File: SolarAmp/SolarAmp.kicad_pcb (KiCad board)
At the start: 2 copper layers, 45.5 x 19 mm, 12 parts, among them J1 Sound Input, J2 Speaker Out, J3 Power Input, U1 TDA2822M

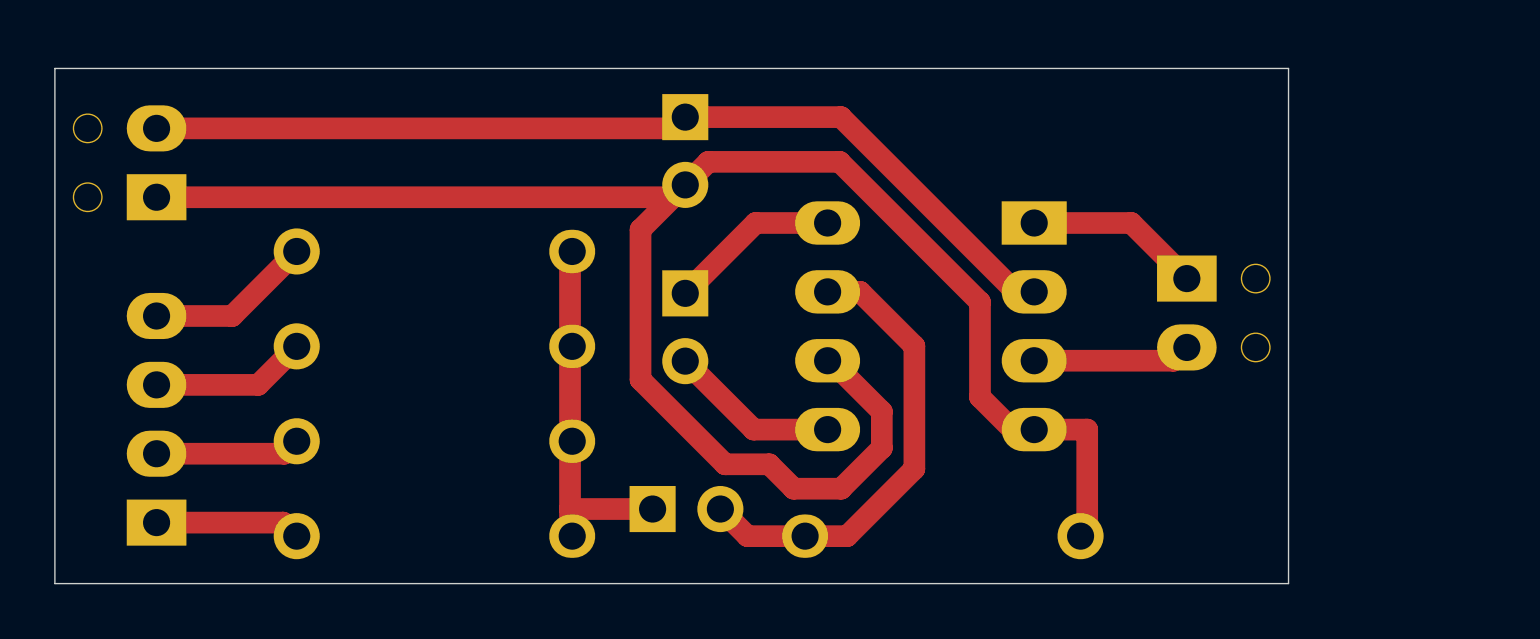
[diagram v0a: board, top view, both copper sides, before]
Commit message: adds power sockets, ground for signal and stronger highpass
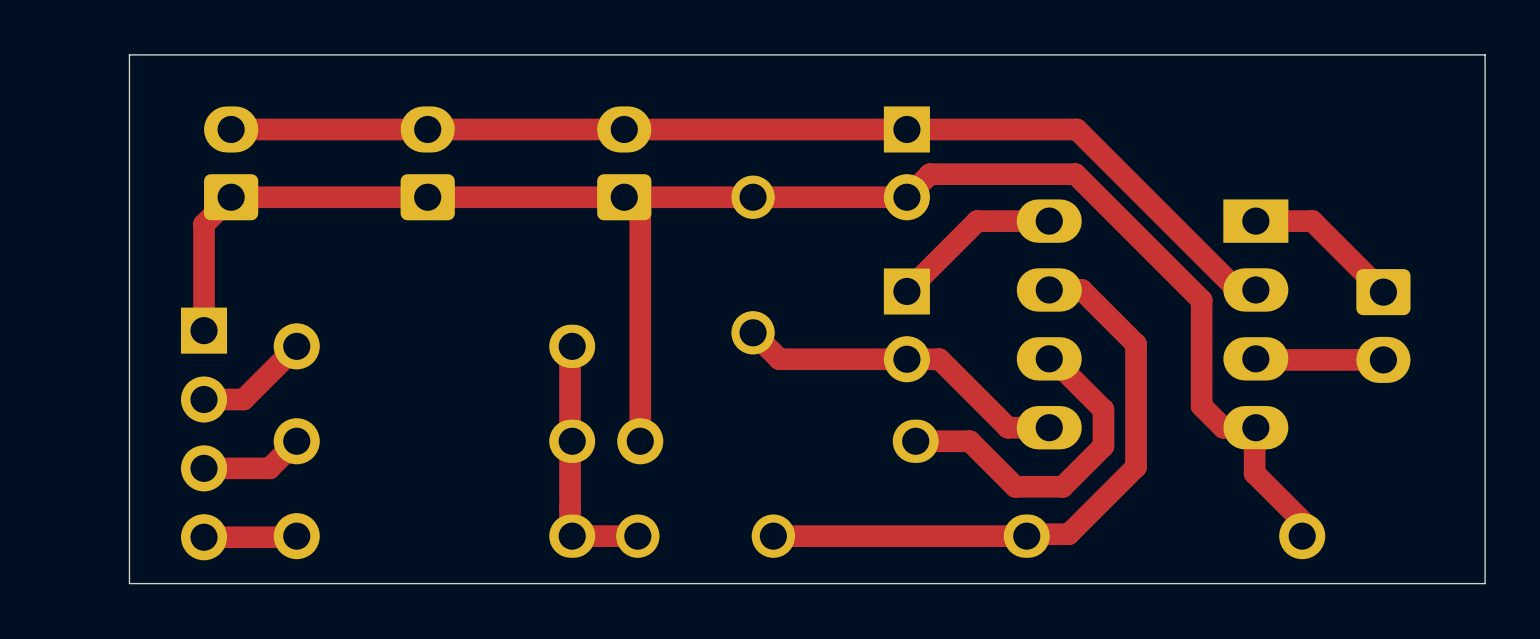
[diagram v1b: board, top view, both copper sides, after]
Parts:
- added C4: 100nF, Capacitor_THT:C_Disc_D5.0mm_W2.5mm_P5.00mm, B.Cu at (107.5, 70.2)
- added J4: Power output, Connector_JST:JST_XH_B2B-XH-A_1x02_P2.50mm_Vertical, B.Cu at (107.0, 57.8)
- added J5: Power in/output, Connector_JST:JST_XH_B2B-XH-A_1x02_P2.50mm_Vertical, B.Cu at (99.8, 57.8)
- C1: value 10u -> 4.7u
- C2: value 10u -> 100nF; footprint Capacitor_THT:CP_Radial_D5.0mm_P2.50mm -> Capacitor_THT:C_Disc_D5.0mm_W2.5mm_P5.00mm
- C3: value 10u -> 47u
- J1: footprint TerminalBlock_Phoenix:TerminalBlock_Phoenix_MPT-0,5-4-2.54_1x04_P2.54mm_Horizontal -> Connector_PinHeader_2.54mm:PinHeader_1x04_P2.54mm_Vertical
- J2: footprint TerminalBlock_Phoenix:TerminalBlock_Phoenix_MPT-0,5-2-2.54_1x02_P2.54mm_Horizontal -> Connector_JST:JST_XH_B2B-XH-A_1x02_P2.50mm_Vertical
- J3: value Power Input -> Power in/output; footprint TerminalBlock_Phoenix:TerminalBlock_Phoenix_MPT-0,5-2-2.54_1x02_P2.54mm_Horizontal -> Connector_JST:JST_XH_B2B-XH-A_1x02_P2.50mm_Vertical
- R5: value 470k -> 10k
- moved R5 14.5 mm to (107.6, 66.8)
- moved C3 8.19 mm to (117.4, 55.2)
- moved C1 8.18 mm to (117.4, 61.2)
- moved U1 8.18 mm to (130.3, 58.6)
- moved R2 8.17 mm to (132.0, 70.2)
- moved C2 7.48 mm to (111.8, 62.8), turned to 90 degrees
- moved J1 7.29 mm to (91.5, 62.7), turned to 180 degrees
- moved J2 7.27 mm to (135.0, 61.2)
- moved J3 2.75 mm to (92.5, 57.8)
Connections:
- C2 pad 1: Net-(C2-Pad1) -> Net-(U1B--)
- C2 pad 2: Net-(U1A-+) -> GND
- J1 pad 1: Net-(J1-Pin_1) -> GND
- R1 pad 1: Net-(J1-Pin_1) -> Net-(J1-Pin_4)
- R1 pad 2: Net-(C2-Pad1) -> Net-(C4-Pad1)
- R3 pad 1: Net-(J1-Pin_2) -> Net-(J1-Pin_3)
- R3 pad 2: Net-(C2-Pad1) -> Net-(C4-Pad1)
- R4 pad 1: Net-(J1-Pin_3) -> Net-(J1-Pin_2)
- R4 pad 2: Net-(C2-Pad1) -> Net-(C4-Pad1)
- R5 pad 1: Net-(J1-Pin_4) -> GND
- R5 pad 2: Net-(C2-Pad1) -> Net-(U1B-+)
- U1 pad 6: GND -> Net-(U1B-+)
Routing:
- net Net-(C2-Pad1): track 13.1 -> 0.00 mm
- net Net-(U1B-+): track 0.00 -> 12.2 mm
- net Net-(C4-Pad1): track 0.00 -> 9.10 mm
- net Net-(U1B--): track 6.30 -> 12.4 mm
- net Net-(U1A-+): track 17.2 -> 23.0 mm
- net Net-(J1-Pin_1): track 5.38 -> 0.00 mm
- net GND: track 67.9 -> 63.4 mm
- net +5V: track 35.2 -> 39.6 mm
- net Net-(J1-Pin_4): track 6.16 -> 3.44 mm
- net Net-(J1-Pin_3): track 5.76 -> 3.83 mm
- net Net-(J1-Pin_2): track 5.36 -> 4.23 mm
- net Net-(J2-Pin_2): track 5.83 -> 4.72 mm
- net Net-(J2-Pin_1): track 6.48 -> 5.79 mm
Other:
- board size 45.5 x 19 mm -> 50 x 19.5 mm
